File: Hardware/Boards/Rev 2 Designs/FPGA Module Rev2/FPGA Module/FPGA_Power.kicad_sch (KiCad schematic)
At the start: 31 parts, among them U1 XCKU3P-FFVA676

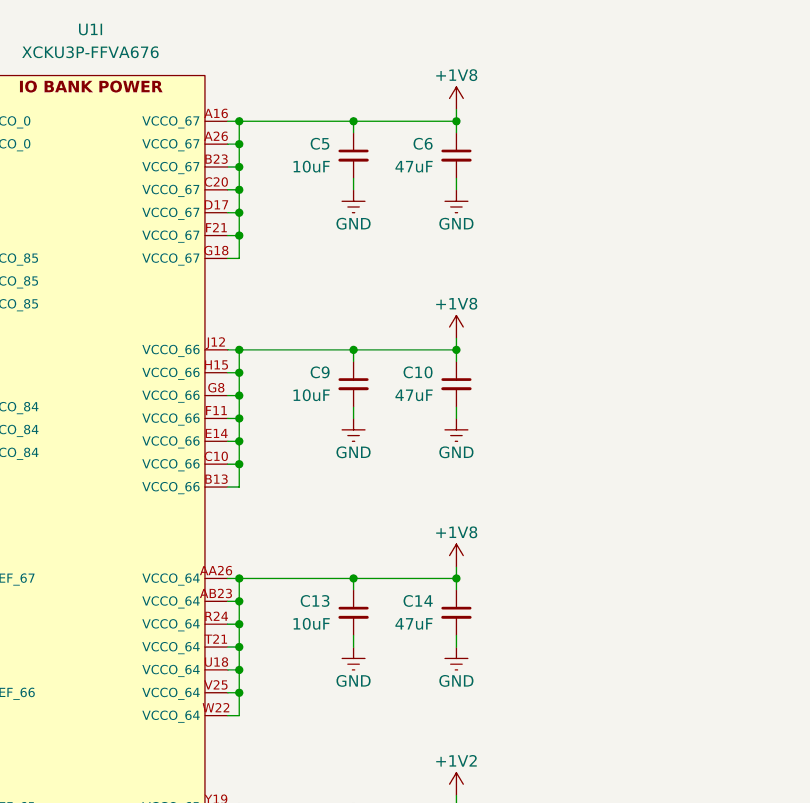
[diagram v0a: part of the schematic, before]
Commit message: modified FPGA MIPI code to add ready output, modified IO module FW to initialize camera after fpga rdy goes high
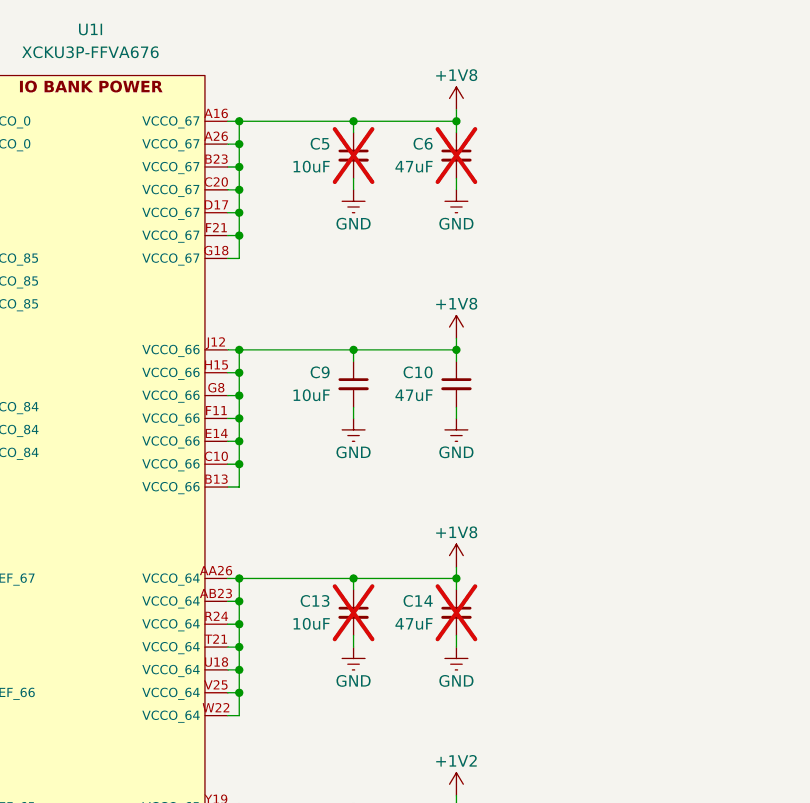
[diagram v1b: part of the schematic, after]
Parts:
- C13, C14, C5, C6: now not fitted
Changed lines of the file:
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@@
 		(in_bom yes)
 		(on_board yes)
-		(dnp no)
+		(dnp yes)
 		(fields_autoplaced yes)
 		(property "Reference" "C13"
@@
 		(in_bom yes)
 		(on_board yes)
-		(dnp no)
+		(dnp yes)
 		(fields_autoplaced yes)
 		(property "Reference" "C5"
@@
 		(in_bom yes)
 		(on_board yes)
-		(dnp no)
+		(dnp yes)
 		(fields_autoplaced yes)
 		(property "Reference" "C6"
@@
 		(in_bom yes)
 		(on_board yes)
-		(dnp no)
+		(dnp yes)
 		(fields_autoplaced yes)
 		(property "Reference" "C14"

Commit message: Added diagrams, papers and presentations
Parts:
- C13, C14, C5, C6: now fitted
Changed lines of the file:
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@@
 (kicad_sch
-	(version 20231120)
+	(version 20250114)
 	(generator "eeschema")
-	(generator_version "8.0")
+	(generator_version "9.0")
 	(paper "A3")
 	(title_block
@@
 	(label "GND"
 		(at 354.33 233.68 90)
-		(fields_autoplaced yes)
 		(effects
 			(font
@@
 		(in_bom yes)
 		(on_board yes)
-		(dnp yes)
+		(dnp no)
 		(fields_autoplaced yes)
 		(property "Reference" "C13"
@@
 		(in_bom yes)
 		(on_board yes)
-		(dnp yes)
+		(dnp no)
 		(fields_autoplaced yes)
 		(property "Reference" "C5"
@@
 		(in_bom yes)
 		(on_board yes)
-		(dnp yes)
+		(dnp no)
 		(fields_autoplaced yes)
 		(property "Reference" "C6"
@@
 		(in_bom yes)
 		(on_board yes)
-		(dnp yes)
+		(dnp no)
 		(fields_autoplaced yes)
 		(property "Reference" "C14"
